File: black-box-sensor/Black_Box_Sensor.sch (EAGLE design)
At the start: 60 parts, among them J1 104031-0811, J2 UX60-MB-5S8, J3 B4B-PH-SM4-TBT(LF)(SN), U1 ADXL375, U2 ADXL375, U3 ATMEGA32U4-AU, U4 ATSAMD21G17A-AUMICROCHIP_TECH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, U5 IAM-20380, U6 NL27WZ32USG, U7 LT1129CST-5#PBF, U8 AD8426ACPZ-WP, U9 TXU0304

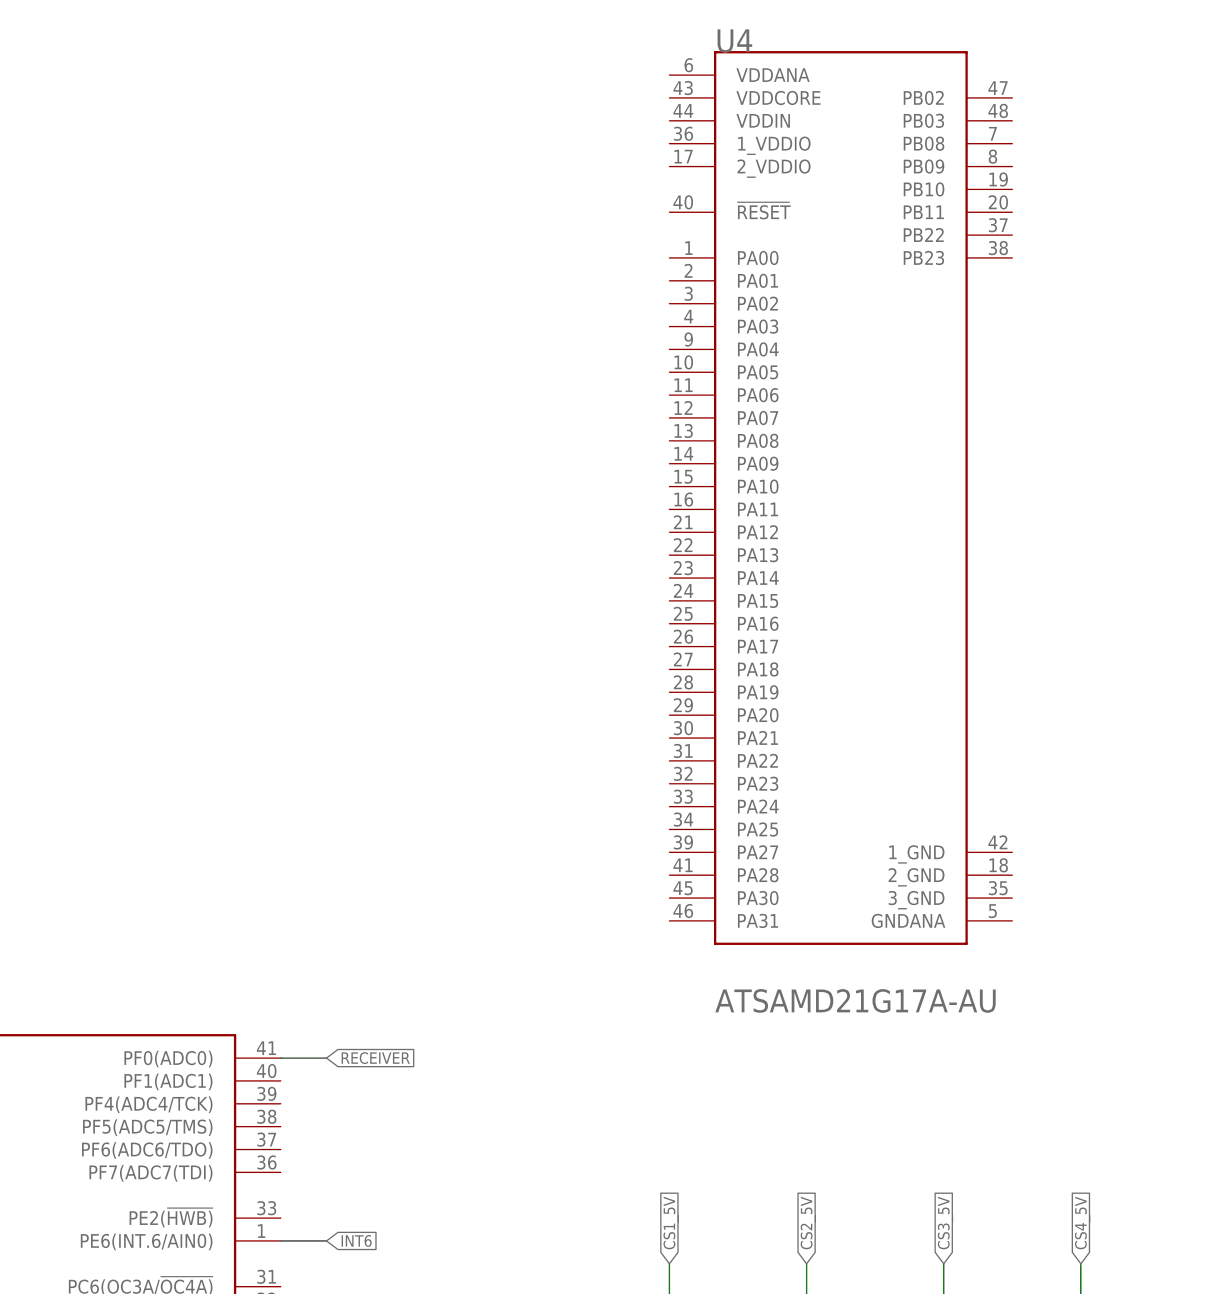
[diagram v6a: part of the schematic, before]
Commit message: begin routing ATSAMD
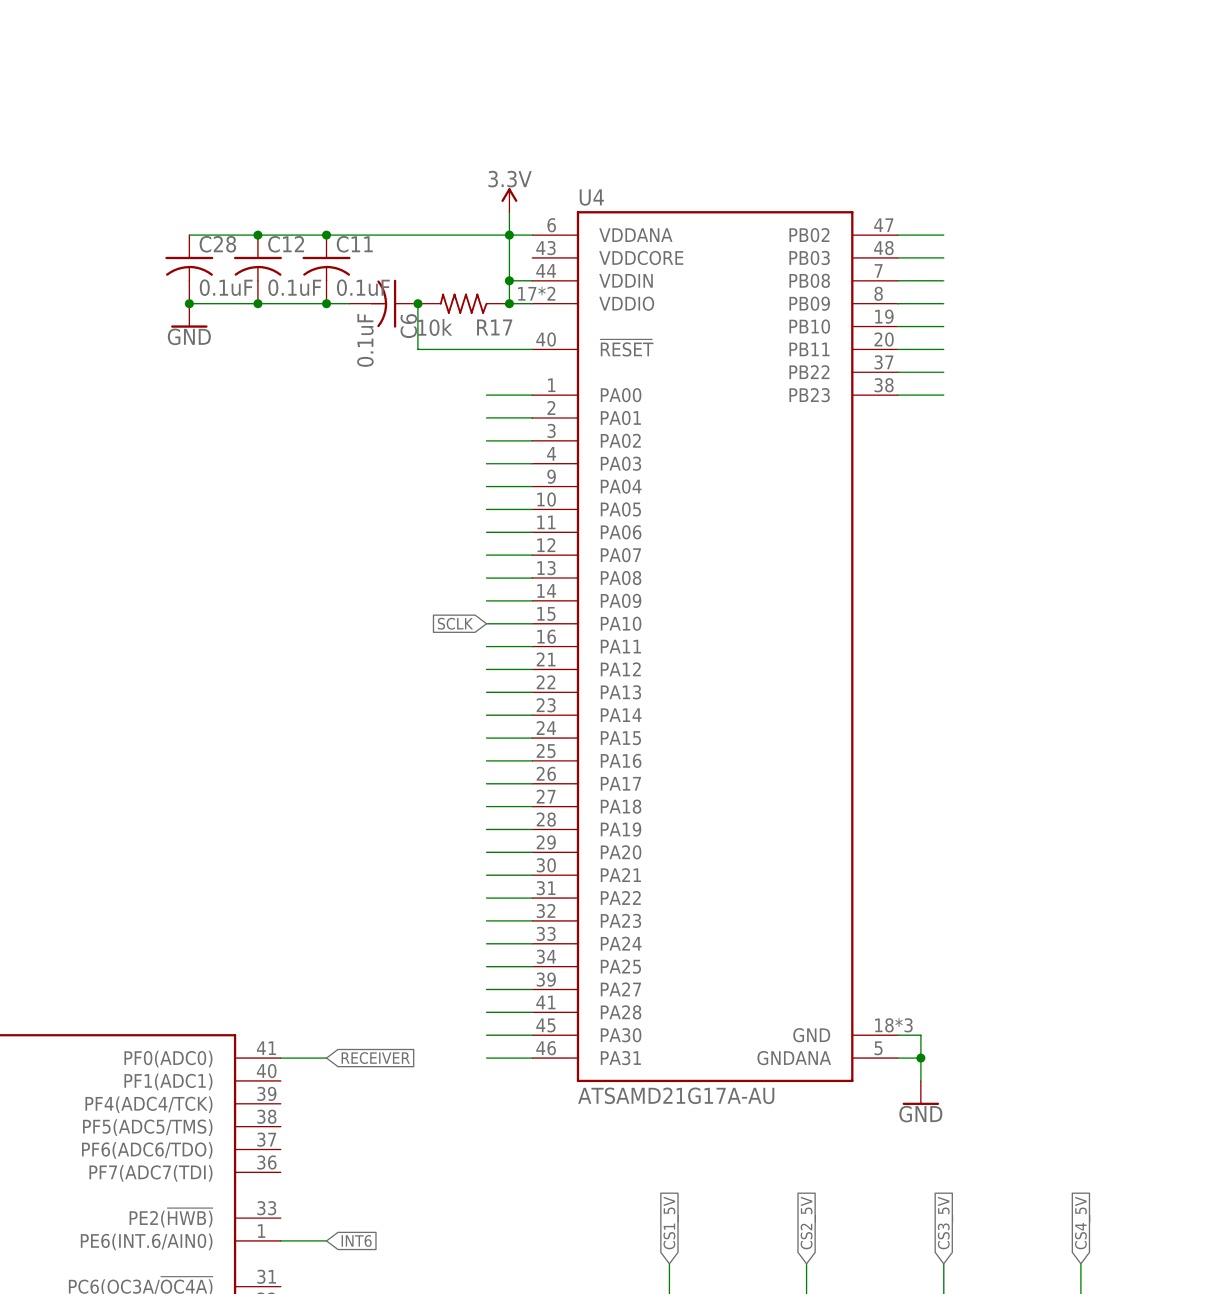
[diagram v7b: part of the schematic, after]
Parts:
- added C11, C12, C28, C6: 0.1uF, rcl:C-USC0603
- added R17: 10k, rcl:R-US_R0603
- U4: value ATSAMD21G17A-AUMICROCHIP_TECHNOLOGY_-_ATMEL_ATSAMD21G17A-AU_0_0 -> ATSAMD21G17A-AU; device BBS_Library:ATSAMD21G17A-AUMICROCHIP_TECHNOLOGY_-_ATMEL_ATSAMD21G17A-AU_0_0 -> BBS_Library:ATSAMD21G17A-AU
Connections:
- new net N$14: C6.1, R17.2, U4.!RESET!
- new net N$15: U4.PA00
- new net N$16: U4.PA01
- new net N$17: U4.PA02
- new net N$18: U4.PA03
- new net N$19: U4.PA04
- new net N$20: U4.PA05
- new net N$21: U4.PA06
- new net N$22: U4.PA07
- new net N$23: U4.PA08
- new net N$24: U4.PA09
- new net N$26: U4.PA11
- new net N$27: U4.PA12
- new net N$28: U4.PA13
- new net N$29: U4.PA14
- new net N$30: U4.PA15
- new net N$31: U4.PA16
- new net N$32: U4.PA17
- new net N$33: U4.PA18
- new net N$34: U4.PA19
- new net N$35: U4.PA20
- new net N$36: U4.PA21
- new net N$37: U4.PA22
- new net N$38: U4.PA23
- new net N$39: U4.PA24
- new net N$40: U4.PA25
- new net N$41: U4.PA27
- new net N$42: U4.PA28
- new net N$43: U4.PA30
- new net N$44: U4.PA31
- new net N$45: U4.PB02
- new net N$46: U4.PB03
- new net N$47: U4.PB08
- new net N$48: U4.PB09
- new net N$49: U4.PB10
- new net N$50: U4.PB11
- new net N$51: U4.PB22
- new net N$52: U4.PB23
- net 3.3V: now also C11.1, C12.1, C28.1, R17.1, U4.VDDANA, U4.VDDIN, U4.VDDIO
- net GND: now also C11.2, C12.2, C28.2, C6.2, U4.GND, U4.GNDANA
- net SCLK: now also U4.PA10

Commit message: finalize for review
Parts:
- removed C10: 1µF, rcl:C-USC0603
- removed C13, C14, C16, C9: 0.1uF, rcl:C-USC0603
- removed C15, C20: 7.5pF, rcl:C-USC0603
- removed R11, R8, R9: 19.3k, rcl:R-US_R0603
- removed R13, R14, R15, R16: 10k, rcl:R-US_R0603
- removed U3: ATMEGA32U4-AU, BBS_Library:ATMEGA32U4-AU
- removed Y1: (no value), SparkFun-Clocks:CRYSTALSMD-3.2X2.5
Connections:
- removed net CS1_5V: R12.2, U3.PB0(SS)
- removed net CS2_5V: R13.2, U3.PB7(OC0A/OC1C/RTS)
- removed net CS3_5V: R14.2, U3.PD4(ICP1/ADC8)
- removed net CS4_5V: R15.2, U3.PD5(XCK/CTS)
- removed net N$14: C6.1, R17.2, U4.!RESET!
- removed net N$15: U4.PA00
- removed net N$16: U4.PA01
- removed net N$17: U4.PA02
- removed net N$18: U4.PA03
- removed net N$19: U4.PA04
- removed net N$20: U4.PA05
- removed net N$21: U4.PA06
- removed net N$22: U4.PA07
- removed net N$23: U4.PA08
- removed net N$24: U4.PA09
- removed net N$26: U4.PA11
- removed net N$27: U4.PA12
- removed net N$28: U4.PA13
- removed net N$29: U4.PA14
- removed net N$30: U4.PA15
- removed net N$31: U4.PA16
- removed net N$32: U4.PA17
- removed net N$33: U4.PA18
- removed net N$34: U4.PA19
- removed net N$35: U4.PA20
- removed net N$36: U4.PA21
- removed net N$37: U4.PA22
- removed net N$38: U4.PA23
- removed net N$39: U4.PA24
- removed net N$40: U4.PA25
- removed net N$41: U4.PA27
- removed net N$42: U4.PA28
- removed net N$43: U4.PA30
- removed net N$44: U4.PA31
- removed net N$45: U4.PB02
- removed net N$46: U4.PB03
- removed net N$47: U4.PB08
- removed net N$48: U4.PB09
- removed net N$49: U4.PB10
- removed net N$50: U4.PB11
- removed net N$51: U4.PB22
- removed net N$52: U4.PB23
- removed net N$7: C15.1, U3.XTAL2, Y1.2
- removed net XTAL1: C20.1, U3.XTAL1, Y1.1
- new net RST: C6.1, R10.2, R12.1, R17.2, U4.!RESET!
- net +5V: no longer C10.1, C13.1, C14.1, C16.1, C9.1, R16.2, U3.AVCC, U3.AVCC1, U3.UCAP, U3.VCC, U3.VCC1
- net 3.3V: no longer U5.CS
- net CS1: now also U4.PA20; no longer R10.2, R12.1
- net CS2: now also U4.PA21; no longer R11.2, R13.1
- net CS3: now also U4.PA22, U5.CS; no longer R14.1, R8.2
- net CS4: now also U4.PA23; no longer R15.1, R9.2
- net CURRENT: now also U4.PA04; no longer U3.PD7(OC4D/ADC10/T0)
- net D+: now also U4.PA25; no longer U3.D+
- net D-: now also U4.PA24; no longer U3.D-
- net FSYNC: now also U4.PA05; no longer U3.PB4(ADC11)
- net GND: no longer C10.2, C13.2, C14.2, C15.2, C16.2, C20.2, C9.2, R11.1, R8.1, R9.1, U3.GND, U3.GND1, U3.GND2, U3.GND3, U3.UGND
- net INT0: now also U4.PA06; no longer U3.PB5(OC1A/ADC12/!OC4B)
- net INT1: now also U4.PA07; no longer U3.PB6(OC1B/OC4B/ADC13)
- net INT2: now also U4.PA09; no longer U3.PD2(INT2/RXD1)
- net INT3: now also U4.PA10; no longer U3.PD3(INT3/TXD1)
- net INT6: now also U4.PA11; no longer U3.PE6(INT.6/AIN0)
- net LED: now also U4.PA02; no longer U3.PD6(T1/ADC9/!OC4D)
- net MISO: now also U4.PA19
- net MISO_5V: no longer U3.PB3(PDO/MISO)
- net MOSI: now also U4.PA16
- net MOSI_5V: no longer U3.PB2(PDI/MOSI)
- net RECEIVER: now also U4.PA03; no longer U3.PF0(ADC0)
- net RST_5V: now also R12.2; no longer R16.1, U3./RESET
- net SCL: now also U4.PB09; no longer U3.PD0(INT0/OC0B/SCL)
- net SCLK: now also U4.PA17; no longer U4.PA10
- net SCLK_5V: no longer U3.PB1(SCK)
- net SDA: now also U4.PB08; no longer U3.PD1(INT1/SDA)
- net VBUS: no longer U3.VBUS
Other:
- moved on the sheet: C11, C12, C27, C28, C6, R17, U4
